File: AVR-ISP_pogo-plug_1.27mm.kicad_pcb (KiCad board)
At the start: 2 copper layers, 12 x 22.5 mm, 4 parts, among them P1 CONN_6, P2 CONN_6

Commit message: Tweaks.
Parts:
- P1: footprint pin_array_3x2 -> my_parts:MADW__PIN_ARRAY_3x2_2.54mm
- turned P1 to 0 degrees
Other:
- net class Default: trace_width 0.2032 -> 0.3048
- net class Power removed
- board text added: "2014"
- board text removed: "2013"

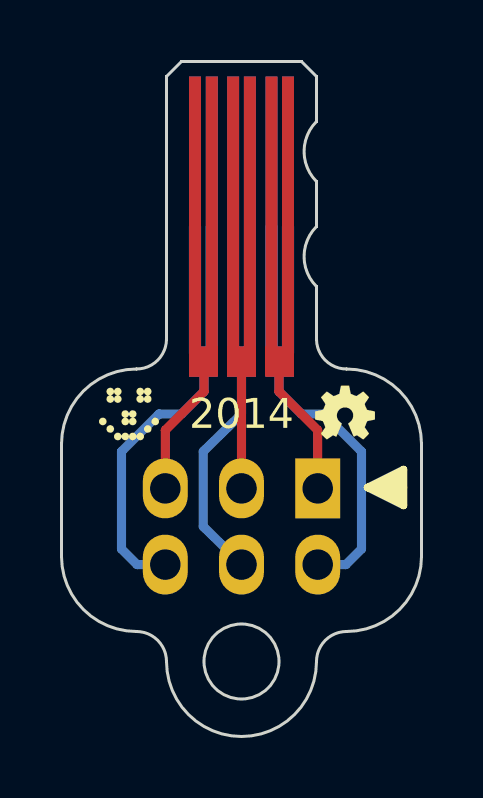
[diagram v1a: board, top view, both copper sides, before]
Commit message: Removed "key-hole" to allow for 90° 3x2 header.
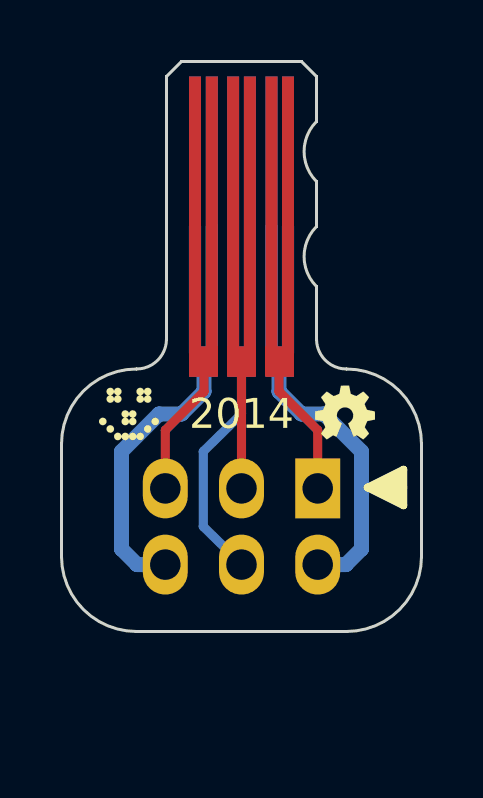
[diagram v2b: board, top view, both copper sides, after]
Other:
- board size 12 x 22.5 mm -> 12 x 19 mm

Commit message: Tweakes pogo footprint. Space for dot of glue.
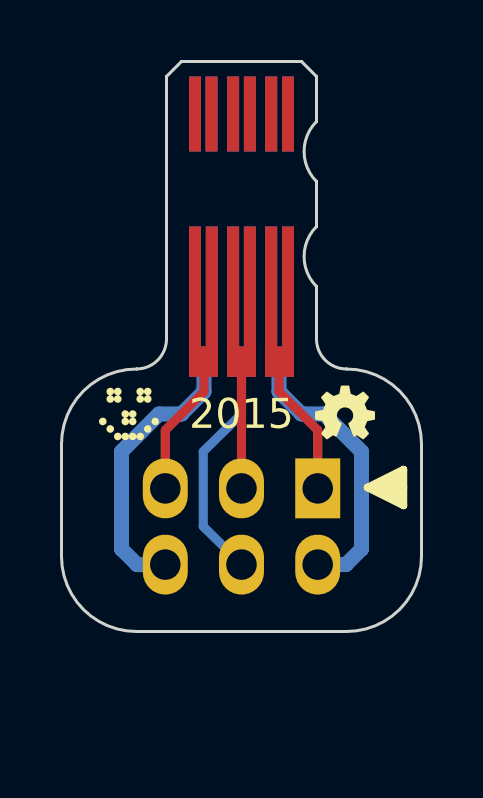
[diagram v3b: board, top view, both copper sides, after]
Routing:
- net /SCK: track 13.5 -> 8.46 mm
- net /RESET: track 14.0 -> 9.00 mm
- net /MOSI: track 17.1 -> 12.1 mm
- net /GND: track 18.7 -> 13.7 mm
- net /V-target: track 18.7 -> 13.7 mm
- net /MISO: track 14.0 -> 9.00 mm
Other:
- board text added: "2015"
- board text removed: "2014"
